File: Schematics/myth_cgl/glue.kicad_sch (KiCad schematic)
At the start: 14 parts, among them U10 74HC00, U3 74LS32, U5 74LS08, U6 74HC04, U7 74HC02, U8 74HC74

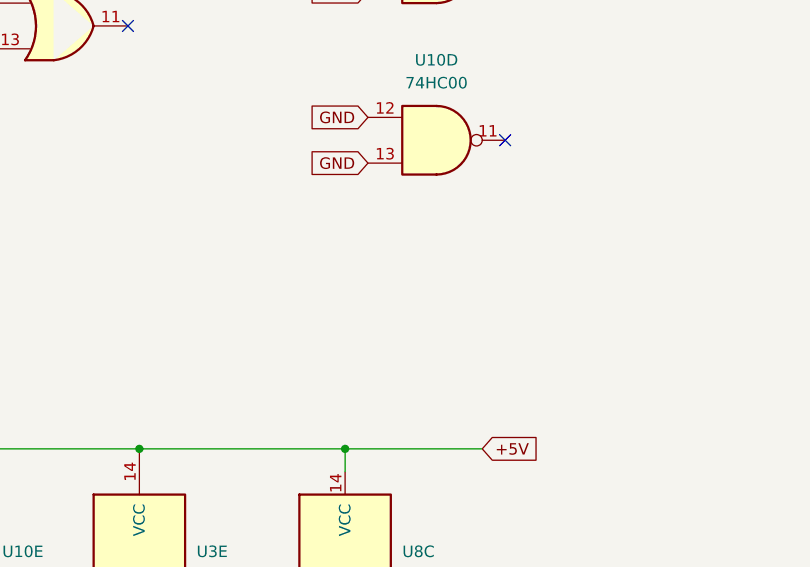
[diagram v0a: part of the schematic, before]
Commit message: Change COR to use R
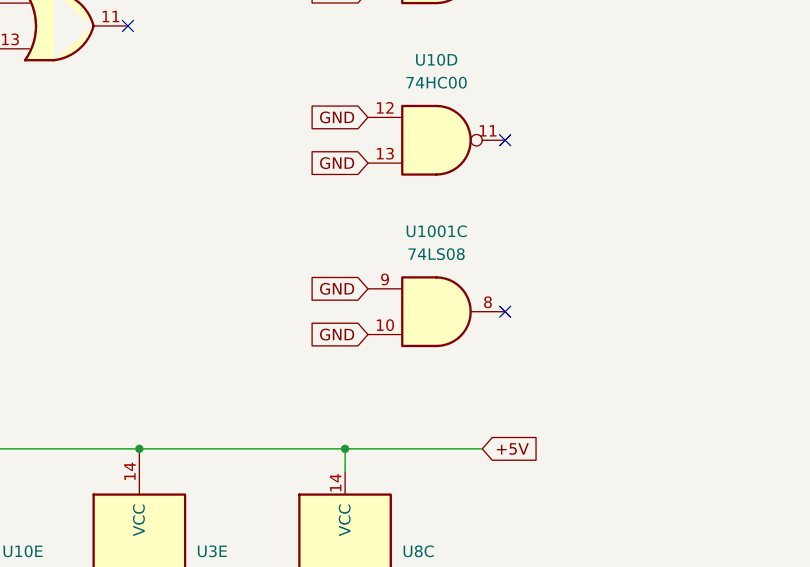
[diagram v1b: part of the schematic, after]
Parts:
- added U1001: 74LS08, Package_DIP:DIP-14_W7.62mm_LongPads, symbol 74xx:74LS08
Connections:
- net GND: now also U1001.10, U1001.9
- no-connect marks 10 -> 11
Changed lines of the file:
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@@
 		(at 171.45 58.42)
 	)
+	(no_connect
+		(at 171.45 114.3)
+	)
 	(wire
 		(pts
@@
 	(global_label "GND"
 		(shape input)
+		(at 156.21 111.76 180)
+		(fields_autoplaced yes)
+		(effects
+			(font
+				(size 1.27 1.27)
+			)
+			(justify right)
+		)
+		(property "Intersheetrefs" "${INTERSHEET_REFS}"
+			(at 149.3543 111.76 0)
+			(effects
+				(font
+					(size 1.27 1.27)
+				)
+				(justify right)
+				(hide yes)
+			)
+		)
+	)
+	(global_label "GND"
+		(shape input)
 		(at 39.37 104.14 180)
 		(fields_autoplaced yes)
@@
 		(property "Intersheetrefs" "${INTERSHEET_REFS}"
 			(at 32.5143 104.14 0)
+			(effects
+				(font
+					(size 1.27 1.27)
+				)
+				(justify right)
+				(hide yes)
+			)
+		)
+	)
+	(global_label "GND"
+		(shape input)
+		(at 156.21 116.84 180)
+		(fields_autoplaced yes)
+		(effects
+			(font
+				(size 1.27 1.27)
+			)
+			(justify right)
+		)
+		(property "Intersheetrefs" "${INTERSHEET_REFS}"
+			(at 149.3543 116.84 0)
 			(effects
 				(font
@@
 				)
 			)
+		)
+	)
+	(symbol
+		(lib_id "74xx:74LS08")
+		(at 163.83 114.3 0)
+		(unit 3)
+		(exclude_from_sim no)
+		(in_bom yes)
+		(on_board yes)
+		(dnp no)
+		(fields_autoplaced yes)
+		(property "Reference" "U1001"
+			(at 163.8217 105.41 0)
+			(effects
+				(font
+					(size 1.27 1.27)
+				)
+			)
+		)
+		(property "Value" "74LS08"
+			(at 163.8217 107.95 0)
+			(effects
+				(font
+					(size 1.27 1.27)
+				)
+			)
+		)
+		(property "Footprint" "Package_DIP:DIP-14_W7.62mm_LongPads"
+			(at 163.83 114.3 0)
+			(effects
+				(font
+					(size 1.27 1.27)
+				)
+				(hide yes)
+			)
+		)
+		(property "Datasheet" "http://www.ti.com/lit/gpn/sn74LS08"
+			(at 163.83 114.3 0)
+			(effects
+				(font
+					(size 1.27 1.27)
+				)
+				(hide yes)
+			)
+		)
+		(property "Description" "Quad And2"
+			(at 163.83 114.3 0)
+			(effects
+				(font
+					(size 1.27 1.27)
+				)
+				(hide yes)
+			)
+		)
+		(pin "2"
+		)
+		(pin "11"
+		)
+		(pin "4"
+		)
+		(pin "12"
+		)
+		(pin "13"
+		)
+		(pin "1"
+		)
+		(pin "3"
+		)
+		(pin "8"
+		)
+		(pin "9"
+		)
+		(pin "5"
+		)
+		(pin "10"
+		)
+		(pin "6"
+		)
+		(pin "14"
+		)
+		(pin "7"
+		)
+		(instances
+			(project "myth_cgl"
+				(path "/fc80d15a-8391-4108-8bee-dfbcee45d6bc/ae006b8b-5cd5-4118-8539-6fcf027a7cfa"
+					(reference "U1001")
+					(unit 3)
+				)
+			)
